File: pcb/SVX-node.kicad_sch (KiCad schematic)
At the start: 35 parts, among them J1 Conn_02x13_Odd_Even, J2 Conn_01x13, J3 Conn_Coaxial, Q1 Q_NPN_BEC, Q2 Q_PNP_BEC, U1 SA818

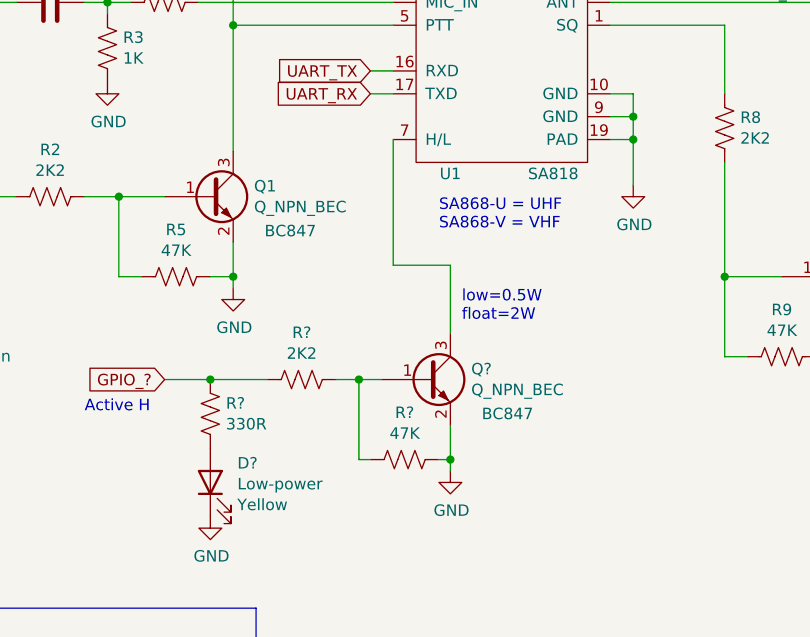
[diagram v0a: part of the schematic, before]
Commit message: fix: replace broken SA818 component with new SA868
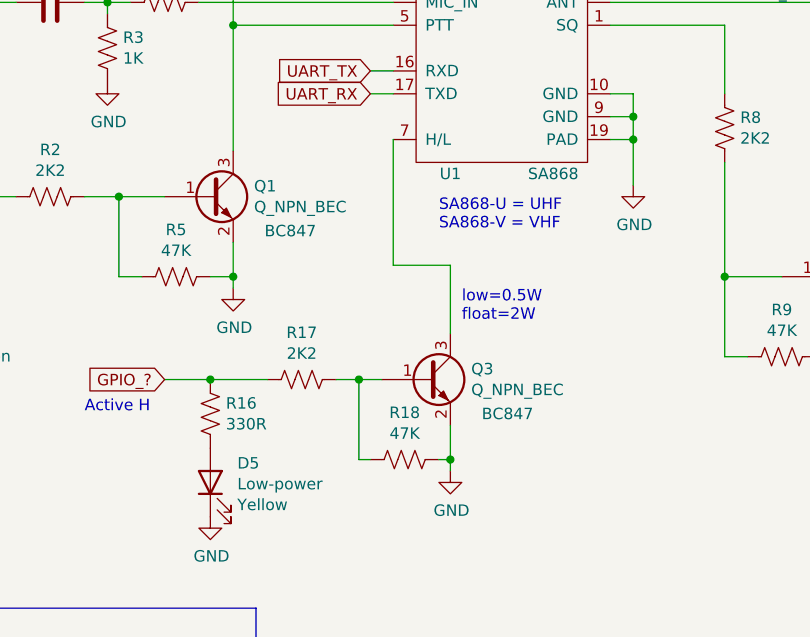
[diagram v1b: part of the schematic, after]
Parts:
- U1: value SA818 -> SA868; footprint Voltlog:SA818 -> SA868:SA868; symbol voltlog:SA818 -> SA868:SA868
- gave numbers to parts that had none: 5
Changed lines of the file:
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@@
     )
   )
-  (symbol (lib_id "voltlog:SA818") (at 135.89 74.93 0) (unit 1)
+  (symbol (lib_id "SA868:SA868") (at 135.89 74.93 0) (unit 1)
     (in_bom yes) (on_board yes)
     (property "Reference" "U1" (id 0) (at 129.54 90.17 0))
-    (property "Value" "SA818" (id 1) (at 140.97 90.17 0))
-    (property "Footprint" "Voltlog:SA818" (id 2) (at 135.89 54.61 0)
+    (property "Value" "SA868" (id 1) (at 140.97 90.17 0))
+    (property "Footprint" "SA868:SA868" (id 2) (at 135.89 54.61 0)
       (effects (font (size 1.27 1.27)) hide)
     )
@@
   (symbol (lib_id "Device:R_US") (at 102.87 116.84 0) (unit 1)
     (in_bom yes) (on_board yes)
-    (property "Reference" "R?" (id 0) (at 104.5972 115.6716 0)
+    (property "Reference" "R16" (id 0) (at 104.5972 115.6716 0)
       (effects (font (size 1.27 1.27)) (justify left))
     )
@@
   (symbol (lib_id "Device:Q_NPN_BEC") (at 127 113.03 0) (unit 1)
     (in_bom yes) (on_board yes)
-    (property "Reference" "Q?" (id 0) (at 131.8514 111.8616 0)
+    (property "Reference" "Q3" (id 0) (at 131.8514 111.8616 0)
       (effects (font (size 1.27 1.27)) (justify left))
     )
@@
   (symbol (lib_id "Device:R_US") (at 124.46 121.92 270) (unit 1)
     (in_bom yes) (on_board yes)
-    (property "Reference" "R?" (id 0) (at 124.46 116.713 90))
+    (property "Reference" "R18" (id 0) (at 124.46 116.713 90))
     (property "Value" "47K" (id 1) (at 124.46 119.0244 90))
     (property "Footprint" "Resistor_SMD:R_0603_1608Metric" (id 2) (at 124.206 122.936 90)
@@
   (symbol (lib_id "Device:LED") (at 102.87 124.46 90) (unit 1)
     (in_bom yes) (on_board yes)
-    (property "Reference" "D?" (id 0) (at 105.8672 122.3264 90)
+    (property "Reference" "D5" (id 0) (at 105.8672 122.3264 90)
       (effects (font (size 1.27 1.27)) (justify right))
     )
@@
   (symbol (lib_id "Device:R_US") (at 113.03 113.03 270) (unit 1)
     (in_bom yes) (on_board yes)
-    (property "Reference" "R?" (id 0) (at 113.03 107.823 90))
+    (property "Reference" "R17" (id 0) (at 113.03 107.823 90))
     (property "Value" "2K2" (id 1) (at 113.03 110.1344 90))
     (property "Footprint" "Resistor_SMD:R_0603_1608Metric" (id 2) (at 112.776 114.046 90)
@@
   (symbol (lib_id "power:GND") (at 129.54 123.19 0) (unit 1)
     (in_bom yes) (on_board yes)
-    (property "Reference" "#PWR?" (id 0) (at 129.54 129.54 0)
+    (property "Reference" "#PWR016" (id 0) (at 129.54 129.54 0)
       (effects (font (size 1.27 1.27)) hide)
     )
@@
   (symbol (lib_id "power:GND") (at 102.87 128.27 0) (unit 1)
     (in_bom yes) (on_board yes)
-    (property "Reference" "#PWR?" (id 0) (at 102.87 134.62 0)
+    (property "Reference" "#PWR015" (id 0) (at 102.87 134.62 0)
       (effects (font (size 1.27 1.27)) hide)
     )
@@
       (reference "#PWR014") (unit 1) (value "GND") (footprint "")
     )
+    (path "/e5eafb5a-3f76-4ebc-97c9-2e3b227c936f"
+      (reference "#PWR015") (unit 1) (value "GND") (footprint "")
+    )
+    (path "/da04dedc-81b6-46a7-8e62-059a9f65ac48"
+      (reference "#PWR016") (unit 1) (value "GND") (footprint "")
+    )
     (path "/fecc8f4a-3557-474d-83f0-6c0ef3972e72"
       (reference "#PWR0102") (unit 1) (value "GND") (footprint "")
     )
-    (path "/da04dedc-81b6-46a7-8e62-059a9f65ac48"
-      (reference "#PWR?") (unit 1) (value "GND") (footprint "")
-    )
-    (path "/e5eafb5a-3f76-4ebc-97c9-2e3b227c936f"
-      (reference "#PWR?") (unit 1) (value "GND") (footprint "")
-    )
     (path "/00000000-0000-0000-0000-00006122876f"
       (reference "C1") (unit 1) (value "470nF") (footprint "Capacitor_SMD:C_0603_1608Metric")
@@
     )
     (path "/ac0d60b3-4852-4109-bba0-5aab2a428165"
-      (reference "D?") (unit 1) (value "Low-power") (footprint "LED_SMD:LED_0603_1608Metric")
+      (reference "D5") (unit 1) (value "Low-power") (footprint "LED_SMD:LED_0603_1608Metric")
     )
     (path "/00000000-0000-0000-0000-000061246236"
@@
     )
     (path "/19925d5b-8424-461c-862a-f1b6fafa53f8"
-      (reference "Q?") (unit 1) (value "Q_NPN_BEC") (footprint "Package_TO_SOT_SMD:SOT-23")
+      (reference "Q3") (unit 1) (value "Q_NPN_BEC") (footprint "Package_TO_SOT_SMD:SOT-23")
     )
     (path "/00000000-0000-0000-0000-0000612264e7"
@@
     )
     (path "/082c63a7-fef0-414e-ba9f-2f63727bccd8"
-      (reference "R?") (unit 1) (value "330R") (footprint "Resistor_SMD:R_0603_1608Metric")
+      (reference "R16") (unit 1) (value "330R") (footprint "Resistor_SMD:R_0603_1608Metric")
+    )
+    (path "/d1762180-b644-48ce-8642-3c552c40b08d"
+      (reference "R17") (unit 1) (value "2K2") (footprint "Resistor_SMD:R_0603_1608Metric")
     )
     (path "/972342e0-e1bf-4c3f-848c-5ad0a2162901"
-      (reference "R?") (unit 1) (value "47K") (footprint "Resistor_SMD:R_0603_1608Metric")
-    )
-    (path "/d1762180-b644-48ce-8642-3c552c40b08d"
-      (reference "R?") (unit 1) (value "2K2") (footprint "Resistor_SMD:R_0603_1608Metric")
+      (reference "R18") (unit 1) (value "47K") (footprint "Resistor_SMD:R_0603_1608Metric")
     )
     (path "/00000000-0000-0000-0000-0000611f7d66"
-      (reference "U1") (unit 1) (value "SA818") (footprint "Voltlog:SA818")
-    )
-  )
+      (reference "U1") (unit 1) (value "SA868") (footprint "SA868:SA868")
+    )
+  )

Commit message: feat: Finalize pcb layout for protoboard assembly
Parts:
- D2: footprint Diode_SMD:D_SMA -> Diode_THT:D_DO-41_SOD81_P5.08mm_Vertical_KathodeUp
- J1: footprint Connector_PinHeader_2.54mm:PinHeader_2x13_P2.54mm_Vertical -> Connector_PinSocket_2.54mm:PinSocket_2x13_P2.54mm_Vertical
- J2: footprint Connector_PinHeader_2.54mm:PinHeader_1x13_P2.54mm_Vertical -> Connector_PinSocket_2.54mm:PinSocket_1x13_P2.54mm_Vertical
- J3: footprint (none) -> Connector_Coaxial:SMA_Amphenol_132291-12_Vertical
- Q1, Q2, Q3: footprint Package_TO_SOT_SMD:SOT-23 -> Package_TO_SOT_THT:TO-92_Inline_Wide
- R9: footprint Resistor_SMD:R_0603_1608Metric -> Resistor_THT:R_Axial_DIN0204_L3.6mm_D1.6mm_P5.08mm_Horizontal
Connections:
- net GPIO_? is gone; now on net GPIO_2: R16.1, R17.2
- net GND: now also U1.11 (GND)
- net GPIO_13: now also R1.1, R2.2
- net GPIO_7: no longer R1.1, R2.2
